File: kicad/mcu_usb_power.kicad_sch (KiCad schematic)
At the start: 41 parts, among them J11 USB4105-GF-A, U16 PCMF3USB3S, U5 MCXN947VDFT

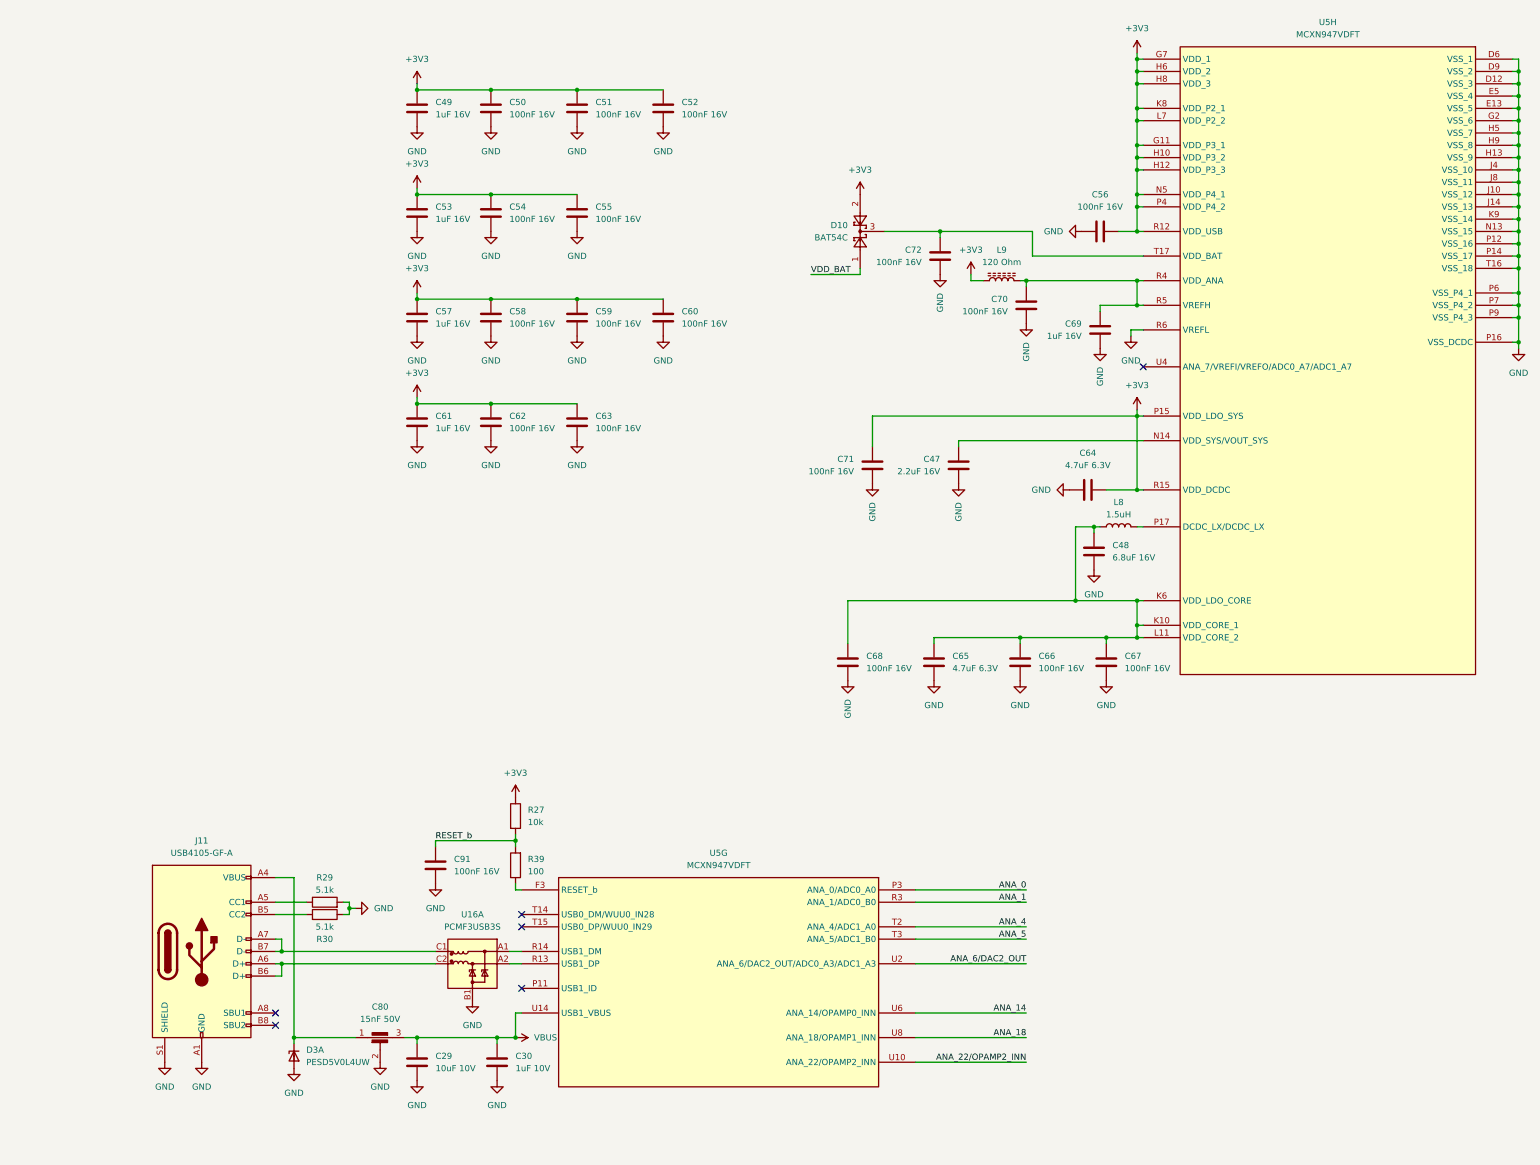
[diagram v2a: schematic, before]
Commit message: Updated schematic and started on layout
- Implemented schematic changes after feedback:
	- BMM350 VDD is 1.8V
	- Replaced net labels with global labels for page references
	- Added 1uF cap to SK9822-EC20
- Added rev-RMII configuration for TJA1103 and DNP resistor to put it in slave mode
- Added TJA1103 PHY address info
- Changed decoupling caps for MCXN to smallest possible packages
- Added traces and vias at MCXN according to guidelines
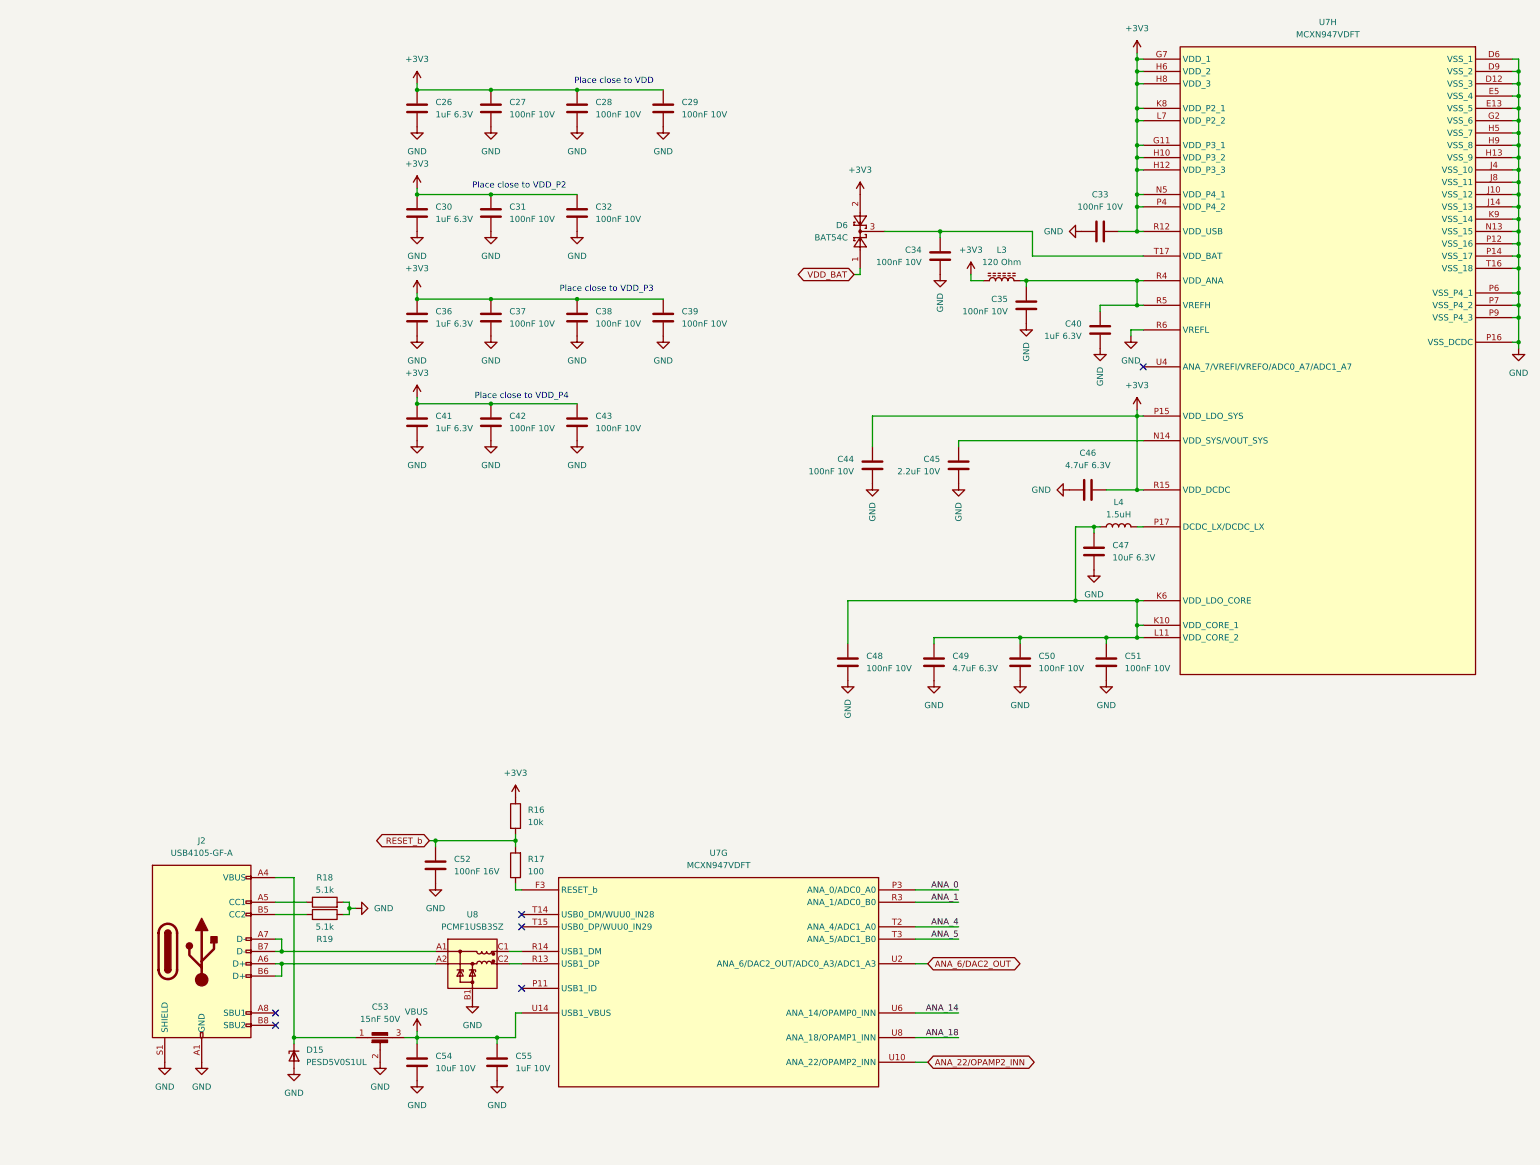
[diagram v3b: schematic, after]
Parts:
- removed D3: PESD5V0L4UW, Package_TO_SOT_SMD:SOT-665, symbol Power_Protection:PESD5V0L4UW
- removed U16: PCMF3USB3S, Package_CSP:Nexperia_WLCSP-15_6-3-6_2.37x1.17mm_Layout6x3_P0.4mm, symbol Power_Protection:PCMF3USB3S
- added D15: PESD5V0S1UL, TVS:PESD5V0S1ULD315, symbol TVS:PESD5V0S1UL
- added U8: PCMF1USB3SZ, TVS:PESD1USB3BCX, symbol TVS:PCMF1USB3SZ
- C26: renamed from C49; value 1uF 16V -> 1uF 6.3V; footprint Capacitor_SMD:C_0603_1608Metric -> Capacitor_SMD:C_0402_1005Metric; MF Samsung Electro-Mechanics -> Murata Electronics; MFPN CL10B105KO8NNNC -> GRM155R70J105KA12D; Supplier PN C59782 -> C88945
- C27: renamed from C50; value 100nF 16V -> 100nF 10V; footprint Capacitor_SMD:C_0402_1005Metric -> Capacitor_SMD:C_0201_0603Metric; MF Samsung Electro-Mechanics -> Murata Electronics; MFPN CL05B104KO5NNNC -> GRM033Z71A104KE14D; Supplier PN C1525 -> C161494
- C28: renamed from C51; value 100nF 16V -> 100nF 10V; footprint Capacitor_SMD:C_0402_1005Metric -> Capacitor_SMD:C_0201_0603Metric; MF Samsung Electro-Mechanics -> Murata Electronics; MFPN CL05B104KO5NNNC -> GRM033Z71A104KE14D; Supplier PN C1525 -> C161494
- C29: renamed from C52; value 100nF 16V -> 100nF 10V; footprint Capacitor_SMD:C_0402_1005Metric -> Capacitor_SMD:C_0201_0603Metric; MF Samsung Electro-Mechanics -> Murata Electronics; MFPN CL05B104KO5NNNC -> GRM033Z71A104KE14D; Supplier PN C1525 -> C161494
- C30: renamed from C53; value 1uF 16V -> 1uF 6.3V; footprint Capacitor_SMD:C_0603_1608Metric -> Capacitor_SMD:C_0402_1005Metric; MF Samsung Electro-Mechanics -> Murata Electronics; MFPN CL10B105KO8NNNC -> GRM155R70J105KA12D; Supplier PN C59782 -> C88945
- C31: renamed from C54; value 100nF 16V -> 100nF 10V; footprint Capacitor_SMD:C_0402_1005Metric -> Capacitor_SMD:C_0201_0603Metric; MF Samsung Electro-Mechanics -> Murata Electronics; MFPN CL05B104KO5NNNC -> GRM033Z71A104KE14D; Supplier PN C1525 -> C161494
- C32: renamed from C55; value 100nF 16V -> 100nF 10V; footprint Capacitor_SMD:C_0402_1005Metric -> Capacitor_SMD:C_0201_0603Metric; MF Samsung Electro-Mechanics -> Murata Electronics; MFPN CL05B104KO5NNNC -> GRM033Z71A104KE14D; Supplier PN C1525 -> C161494
- C33: renamed from C56; value 100nF 16V -> 100nF 10V; footprint Capacitor_SMD:C_0402_1005Metric -> Capacitor_SMD:C_0201_0603Metric; MF Samsung Electro-Mechanics -> Murata Electronics; MFPN CL05B104KO5NNNC -> GRM033Z71A104KE14D; Supplier PN C1525 -> C161494
- C34: renamed from C72; value 100nF 16V -> 100nF 10V; footprint Capacitor_SMD:C_0402_1005Metric -> Capacitor_SMD:C_0201_0603Metric; MF Samsung Electro-Mechanics -> Murata Electronics; MFPN CL05B104KO5NNNC -> GRM033Z71A104KE14D; Supplier PN C1525 -> C161494
- C35: renamed from C70; value 100nF 16V -> 100nF 10V; footprint Capacitor_SMD:C_0402_1005Metric -> Capacitor_SMD:C_0201_0603Metric; MF Samsung Electro-Mechanics -> Murata Electronics; MFPN CL05B104KO5NNNC -> GRM033Z71A104KE14D; Supplier PN C1525 -> C161494
- C36: renamed from C57; value 1uF 16V -> 1uF 6.3V; footprint Capacitor_SMD:C_0603_1608Metric -> Capacitor_SMD:C_0402_1005Metric; MF Samsung Electro-Mechanics -> Murata Electronics; MFPN CL10B105KO8NNNC -> GRM155R70J105KA12D; Supplier PN C59782 -> C88945
- C37: renamed from C58; value 100nF 16V -> 100nF 10V; footprint Capacitor_SMD:C_0402_1005Metric -> Capacitor_SMD:C_0201_0603Metric; MF Samsung Electro-Mechanics -> Murata Electronics; MFPN CL05B104KO5NNNC -> GRM033Z71A104KE14D; Supplier PN C1525 -> C161494
- C38: renamed from C59; value 100nF 16V -> 100nF 10V; footprint Capacitor_SMD:C_0402_1005Metric -> Capacitor_SMD:C_0201_0603Metric; MF Samsung Electro-Mechanics -> Murata Electronics; MFPN CL05B104KO5NNNC -> GRM033Z71A104KE14D; Supplier PN C1525 -> C161494
- C39: renamed from C60; value 100nF 16V -> 100nF 10V; footprint Capacitor_SMD:C_0402_1005Metric -> Capacitor_SMD:C_0201_0603Metric; MF Samsung Electro-Mechanics -> Murata Electronics; MFPN CL05B104KO5NNNC -> GRM033Z71A104KE14D; Supplier PN C1525 -> C161494
- C40: renamed from C69; value 1uF 16V -> 1uF 6.3V; footprint Capacitor_SMD:C_0603_1608Metric -> Capacitor_SMD:C_0402_1005Metric; MF Samsung Electro-Mechanics -> Murata Electronics; MFPN CL10B105KO8NNNC -> GRM155R70J105KA12D; Supplier PN C59782 -> C88945
- C41: renamed from C61; value 1uF 16V -> 1uF 6.3V; footprint Capacitor_SMD:C_0603_1608Metric -> Capacitor_SMD:C_0402_1005Metric; MF Samsung Electro-Mechanics -> Murata Electronics; MFPN CL10B105KO8NNNC -> GRM155R70J105KA12D; Supplier PN C59782 -> C88945
- C42: renamed from C62; value 100nF 16V -> 100nF 10V; footprint Capacitor_SMD:C_0402_1005Metric -> Capacitor_SMD:C_0201_0603Metric; MF Samsung Electro-Mechanics -> Murata Electronics; MFPN CL05B104KO5NNNC -> GRM033Z71A104KE14D; Supplier PN C1525 -> C161494
- C43: renamed from C63; value 100nF 16V -> 100nF 10V; footprint Capacitor_SMD:C_0402_1005Metric -> Capacitor_SMD:C_0201_0603Metric; MF Samsung Electro-Mechanics -> Murata Electronics; MFPN CL05B104KO5NNNC -> GRM033Z71A104KE14D; Supplier PN C1525 -> C161494
- C44: renamed from C71; value 100nF 16V -> 100nF 10V; footprint Capacitor_SMD:C_0402_1005Metric -> Capacitor_SMD:C_0201_0603Metric; MF Samsung Electro-Mechanics -> Murata Electronics; MFPN CL05B104KO5NNNC -> GRM033Z71A104KE14D; Supplier PN C1525 -> C161494
- C45: renamed from C47; value 2.2uF 16V -> 2.2uF 10V; footprint Capacitor_SMD:C_0805_2012Metric -> Capacitor_SMD:C_0402_1005Metric; MF Samsung Electro-Mechanics -> Murata Electronics; MFPN CL21B225KAFNNNE -> GRM155Z71A225KE44D; Supplier JLCPCB -> DigiKey; Supplier PN C19110 -> 490-GRM155Z71A225KE44DCT-ND
- C47: renamed from C48; value 6.8uF 16V -> 10uF 6.3V; footprint Capacitor_SMD:C_1206_3216Metric -> Capacitor_SMD:C_0603_1608Metric; MF TDK -> Murata Electronics; MFPN C3216X7R1V685KT000E -> GRM188Z71A106KA73D; Supplier PN C342646 -> C2959727
- C48: renamed from C68; value 100nF 16V -> 100nF 10V; footprint Capacitor_SMD:C_0402_1005Metric -> Capacitor_SMD:C_0201_0603Metric; MF Samsung Electro-Mechanics -> Murata Electronics; MFPN CL05B104KO5NNNC -> GRM033Z71A104KE14D; Supplier PN C1525 -> C161494
- C50: renamed from C66; value 100nF 16V -> 100nF 10V; footprint Capacitor_SMD:C_0402_1005Metric -> Capacitor_SMD:C_0201_0603Metric; MF Samsung Electro-Mechanics -> Murata Electronics; MFPN CL05B104KO5NNNC -> GRM033Z71A104KE14D; Supplier PN C1525 -> C161494
- C51: renamed from C67; value 100nF 16V -> 100nF 10V; footprint Capacitor_SMD:C_0402_1005Metric -> Capacitor_SMD:C_0201_0603Metric; MF Samsung Electro-Mechanics -> Murata Electronics; MFPN CL05B104KO5NNNC -> GRM033Z71A104KE14D; Supplier PN C1525 -> C161494
- renumbered C64 to C46, C65 to C49, C91 to C52, C80 to C53, C29 to C54, C30 to C55, D10 to D6, J11 to J2, L9 to L3, L8 to L4, R27 to R16, R39 to R17, R29 to R18, R30 to R19, U5 to U7
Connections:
- net GND: now also D15.2 (A), U8.B1 (GND_CH1)
- net at U7.R14 (USB1_DM): now also U8.C1 (CH1_OUT+)
- net at U7.R13 (USB1_DP): now also U8.C2 (CH1_OUT-)
- net at J2.A7 (D-), J2.B7 (D-): now also U8.A1 (CH1_IN+)
- net at J2.A6 (D+), J2.B6 (D+): now also U8.A2 (CH1_IN-)
- net at C53.1, J2.A4 (VBUS), J2.A9 (VBUS)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: now also D15.1 (K1)
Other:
- note added: "Place close to VDD"
- note added: "Place close to VDD_P2"
- note added: "Place close to VDD_P3"
- note added: "Place close to VDD_P4"

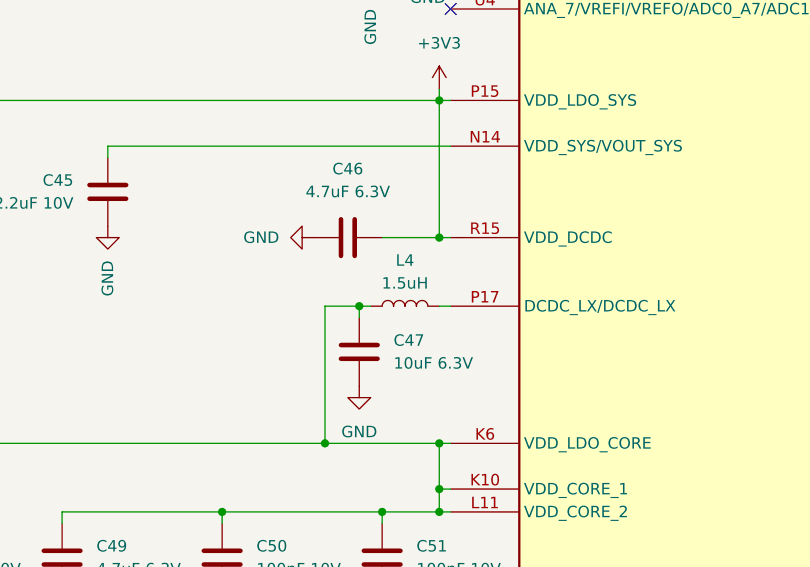
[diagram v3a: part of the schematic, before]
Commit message: Updated PCB layout
- Placed decoupling caps at MCXN with traces.
- Grouped parts of schematic.
- Started positioning Power components
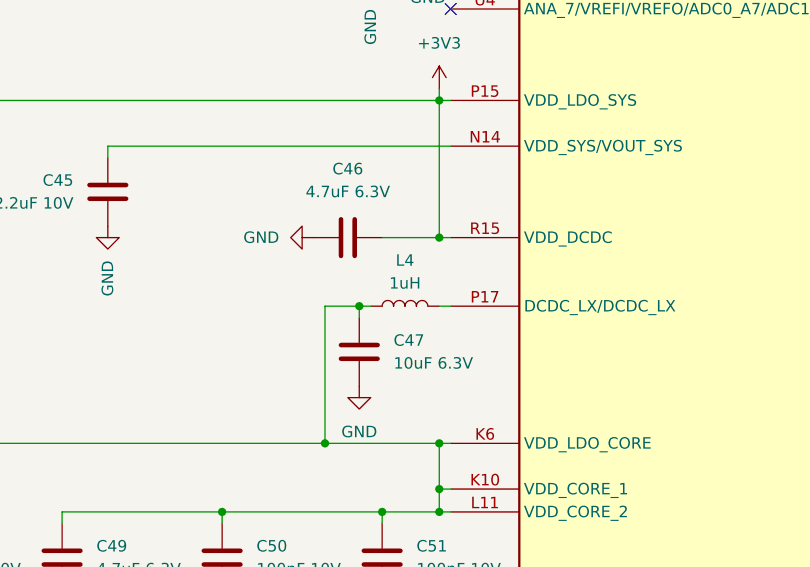
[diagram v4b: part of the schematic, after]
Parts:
- L4: value 1.5uH -> 1uH; footprint Inductor_SMD:L_1008_2520Metric -> Inductor_SMD:L_0603_1608Metric; MF Murata Electronics -> Taiyo Yuden; MFPN DFE252012P-1R5M=P2 -> MCKK1608T1R0MN; Supplier DigiKey -> JLCPCB; Supplier PN 490-10648-1-ND -> C5669778
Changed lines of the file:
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@@
 			)
 		)
-		(property "Value" "1.5uH"
+		(property "Value" "1uH"
 			(at 264.16 138.43 90)
 			(effects
@@
 			)
 		)
-		(property "Footprint" "Inductor_SMD:L_1008_2520Metric"
+		(property "Footprint" "Inductor_SMD:L_0603_1608Metric"
 			(at 264.16 140.97 0)
 			(effects
@@
 			)
 		)
-		(property "Datasheet" "https://www.murata.com/~/media/webrenewal/products/inductor/chip/tokoproducts/wirewoundmetalalloychiptype/m_dfe252012p.ashx"
+		(property "Datasheet" "https://mm.digikey.com/Volume0/opasdata/d220001/medias/docus/2268/MCKK1608T1R0MN_SS.pdf"
 			(at 264.16 140.97 0)
 			(effects
@@
 			)
 		)
-		(property "Description" "FIXED IND 1.5UH 2.6A 0.06OHM SMD"
+		(property "Description" "1.3A 1uH ±20% 2A 123mΩ 0603 Inductors (SMD) ROHS"
 			(at 264.16 140.97 0)
 			(effects
@@
 			)
 		)
-		(property "MF" "Murata Electronics"
+		(property "MF" "Taiyo Yuden"
 			(at 264.16 140.97 0)
 			(effects
@@
 			)
 		)
-		(property "MFPN" "DFE252012P-1R5M=P2"
+		(property "MFPN" "MCKK1608T1R0MN"
 			(at 264.16 140.97 0)
 			(effects
@@
 			)
 		)
-		(property "Supplier" "DigiKey"
+		(property "Supplier" "JLCPCB"
 			(at 264.16 140.97 0)
 			(effects
@@
 			)
 		)
-		(property "Supplier PN" "490-10648-1-ND"
+		(property "Supplier PN" "C5669778"
 			(at 264.16 140.97 0)
 			(effects
-				(font
-					(size 1.27 1.27)
-				)
-				(hide yes)
-			)
-		)
-		(property "MANUFACTURER" ""
-			(at 264.16 140.97 0)
-			(effects
-				(font
-					(size 1.27 1.27)
-				)
-				(hide yes)
-			)
-		)
-		(property "MAXIMUM_PACKAGE_HEIGHT" ""
-			(at 264.16 140.97 0)
-			(effects
-				(font
-					(size 1.27 1.27)
-				)
-				(hide yes)
-			)
-		)
-		(property "PARTREV" ""
-			(at 264.16 140.97 0)
-			(effects
-				(font
-					(size 1.27 1.27)
-				)
-				(hide yes)
-			)
-		)
-		(property "STANDARD" ""
-			(at 264.16 140.97 0)
-			(effects
